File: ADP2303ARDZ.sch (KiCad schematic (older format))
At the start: 17 parts, among them P1 CONN_01X03, P2 CONN_01X03, U1 ADP2303ARDZ-5.0, U2 MCP1825S

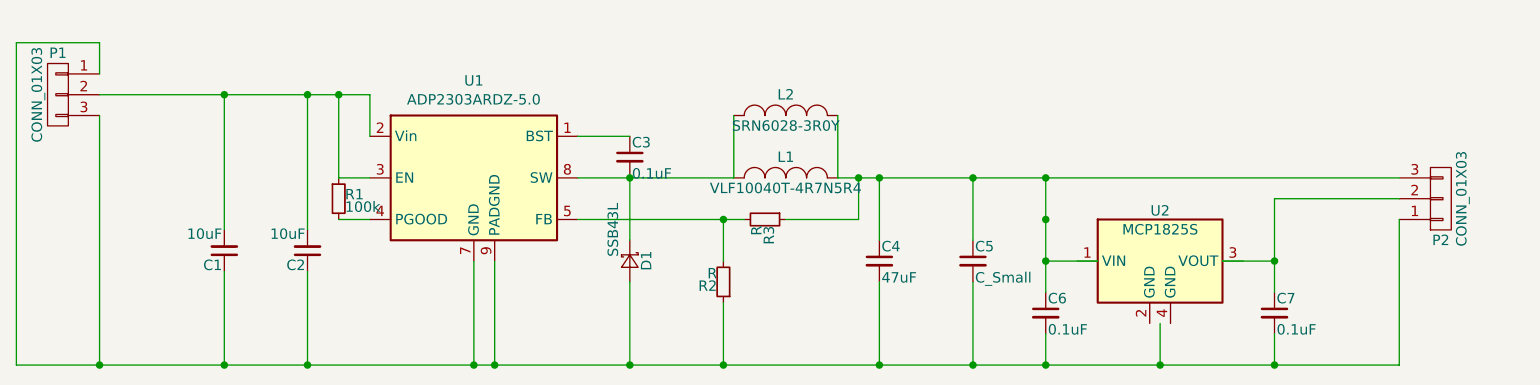
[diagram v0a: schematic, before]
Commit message: Changed design to use local componenet libs
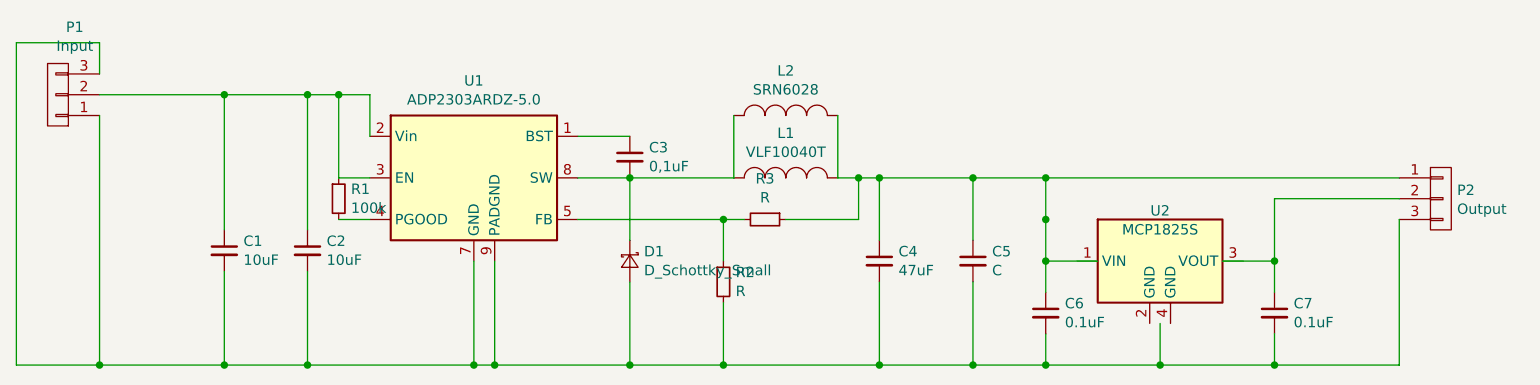
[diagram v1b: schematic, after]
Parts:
- C1, C2, C4, C6, C7: footprint Capacitor_SMD:C_0603_1608Metric_Pad0.84x1.00mm_HandSolder -> (none)
- C3: value 0.1uF -> 0,1uF; footprint Capacitor_SMD:C_0603_1608Metric_Pad0.84x1.00mm_HandSolder -> (none)
- C5: value C_Small -> C; footprint Capacitor_SMD:C_0603_1608Metric_Pad0.84x1.00mm_HandSolder -> (none)
- D1: value SSB43L -> D_Schottky_Small; footprint Diode_SMD:D_SMB_Handsoldering -> (none)
- L1: value VLF10040T-4R7N5R4 -> VLF10040T; footprint Inductor_SMD:L_TDK_VLF10040 -> (none)
- L2: value SRN6028-3R0Y -> SRN6028; footprint Inductor_SMD:L_Bourns-SRN6028 -> (none)
- P1: value CONN_01X03 -> Input; footprint Conn_PinSocket_2.54mm:PinSocket_1x03_P2.54mm_Vertical -> (none)
- P2: value CONN_01X03 -> Output; footprint Conn_PinSocket_2.54mm:PinSocket_1x03_P2.54mm_Vertical -> (none)
- R1, R2, R3: footprint Resistor_SMD:R_0603_1608Metric_Pad0.84x1.00mm_HandSolder -> (none)
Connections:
- wire segments 41 -> 65

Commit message: Selected local footprints for the design
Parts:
- C1, C2, C3, C4, C5, C6, C7: footprint (none) -> footprints:C_0603_1608Metric
- D1: footprint (none) -> footprints:D_SMB_Handsoldering
- L1: footprint (none) -> footprints:L_TDK_VLF10040
- L2: footprint (none) -> footprints:L_Bourns-SRN6028
- P1, P2: footprint (none) -> footprints:PinSocket_1x03_P2.54mm_Vertical
- R1, R2, R3: footprint (none) -> footprints:R_0603_1608Metric
- U1: footprint Housings_SOIC:SOIC-8-1EP_3.9x4.9mm_Pitch1.27mm -> footprints:SOIC-8-1EP_3.9x4.9mm_Pitch1.27mm
- U2: footprint (none) -> footprints:SOT-223
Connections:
- wire segments 65 -> 41
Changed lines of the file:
@@
 Connection ~ 5250 4300
 Wire Wire Line
-	6550 3400 6800 3400
-Wire Wire Line
-	6800 3400 7300 3400
+	6550 3400 7300 3400
 Wire Wire Line
 	6800 3200 6550 3200
@@
 	7300 3400 7300 3100
 Wire Wire Line
-	7800 3400 7900 3400
-Wire Wire Line
-	7900 3400 8000 3400
-Wire Wire Line
-	8000 3400 8450 3400
-Wire Wire Line
-	8450 3400 8800 3400
-Wire Wire Line
-	8800 3400 10500 3400
+	7800 3400 10500 3400
 Wire Wire Line
 	7800 3400 7800 3100
@@
 	8800 3800 9050 3800
 Wire Wire Line
-	8800 3400 8800 3600
-Wire Wire Line
-	8800 3600 8800 3800
-Wire Wire Line
-	8800 3800 8800 3950
+	8800 3400 8800 3950
 Connection ~ 8800 3400
 Wire Wire Line
@@
 	9650 3800 9900 3800
 Wire Wire Line
-	9900 3500 9900 3800
-Wire Wire Line
-	9900 3800 9900 3950
+	9900 3500 9900 3950
 Wire Wire Line
 	9900 3500 10500 3500
@@
 	3850 2750 3850 4300
 Wire Wire Line
-	3850 4300 4250 4300
-Wire Wire Line
-	4250 4300 4850 4300
-Wire Wire Line
-	4850 4300 5250 4300
-Wire Wire Line
-	5250 4300 6050 4300
-Wire Wire Line
-	6050 4300 6150 4300
-Wire Wire Line
-	6150 4300 6800 4300
-Wire Wire Line
-	6800 4300 7250 4300
-Wire Wire Line
-	7250 4300 8000 4300
-Wire Wire Line
-	8000 4300 8450 4300
-Wire Wire Line
-	8450 4300 8800 4300
-Wire Wire Line
-	8800 4300 9350 4300
-Wire Wire Line
-	9350 4300 9900 4300
-Wire Wire Line
-	9900 4300 10500 4300
-Wire Wire Line
-	4250 3000 4850 3000
-Wire Wire Line
-	4850 3000 5250 3000
-Wire Wire Line
-	5250 3000 5400 3000
-Wire Wire Line
-	5400 3000 5550 3000
+	3850 4300 10500 4300
+Wire Wire Line
+	4250 3000 5550 3000
 Wire Wire Line
 	5550 3000 5550 3200
@@
 Connection ~ 9350 4300
 Wire Wire Line
-	6550 3600 7250 3600
-Wire Wire Line
-	7250 3600 7350 3600
+	6550 3600 7350 3600
 Wire Wire Line
 	7550 3600 7900 3600
@@
 F 0 "P1" H 3969 2675 50  0000 C CNN
 F 1 "Input" H 3969 2766 50  0000 C CNN
-F 2 "" H 4050 3000 50  0000 C CNN
+F 2 "footprints:PinSocket_1x03_P2.54mm_Vertical" H 4050 3000 50  0001 C CNN
 F 3 "" H 4050 3000 50  0000 C CNN
 	1    4050 3000
@@
 F 0 "C1" H 4942 3796 50  0000 L CNN
 F 1 "10uF" H 4942 3705 50  0000 L CNN
-F 2 "" H 4850 3750 50  0001 C CNN
+F 2 "footprints:C_0603_1608Metric" H 4850 3750 50  0001 C CNN
 F 3 "" H 4850 3750 50  0001 C CNN
 	1    4850 3750
@@
 F 0 "C2" H 5342 3796 50  0000 L CNN
 F 1 "10uF" H 5342 3705 50  0000 L CNN
-F 2 "" H 5250 3750 50  0001 C CNN
+F 2 "footprints:C_0603_1608Metric" H 5250 3750 50  0001 C CNN
 F 3 "" H 5250 3750 50  0001 C CNN
 	1    5250 3750
@@
 F 0 "R1" H 5459 3546 50  0000 L CNN
 F 1 "100k" H 5459 3455 50  0000 L CNN
-F 2 "" H 5400 3500 50  0001 C CNN
+F 2 "footprints:R_0603_1608Metric" H 5400 3500 50  0001 C CNN
 F 3 "" H 5400 3500 50  0001 C CNN
 	1    5400 3500
@@
 F 0 "U1" H 6050 3867 50  0000 C CNN
 F 1 "ADP2303ARDZ-5.0" H 6050 3776 50  0000 C CNN
-F 2 "Housings_SOIC:SOIC-8-1EP_3.9x4.9mm_Pitch1.27mm" H 6200 3050 50  0001 L CNN
+F 2 "footprints:SOIC-8-1EP_3.9x4.9mm_Pitch1.27mm" H 6200 3050 50  0001 L CNN
 F 3 "http://www.analog.com/media/en/technical-documentation/data-sheets/ADP2302_2303.pdf" H 5850 4000 50  0001 C CNN
 	1    6050 3400
@@
 F 0 "C3" H 6892 3346 50  0000 L CNN
 F 1 "0,1uF" H 6892 3255 50  0000 L CNN
-F 2 "" H 6800 3300 50  0001 C CNN
+F 2 "footprints:C_0603_1608Metric" H 6800 3300 50  0001 C CNN
 F 3 "" H 6800 3300 50  0001 C CNN
 	1    6800 3300
@@
 F 0 "D1" V 6754 3868 50  0000 L CNN
 F 1 "D_Schottky_Small" V 6845 3868 50  0000 L CNN
-F 2 "" V 6800 3800 50  0001 C CNN
+F 2 "footprints:D_SMB_Handsoldering" V 6800 3800 50  0001 C CNN
 F 3 "" V 6800 3800 50  0001 C CNN
 	1    6800 3800
@@
 F 0 "R2" H 7309 3946 50  0000 L CNN
 F 1 "R" H 7309 3855 50  0000 L CNN
-F 2 "" H 7250 3900 50  0001 C CNN
+F 2 "footprints:R_0603_1608Metric" H 7250 3900 50  0001 C CNN
 F 3 "" H 7250 3900 50  0001 C CNN
 	1    7250 3900
@@
 F 0 "R3" V 7254 3600 50  0000 C CNN
 F 1 "R" V 7345 3600 50  0000 C CNN
-F 2 "" H 7450 3600 50  0001 C CNN
+F 2 "footprints:R_0603_1608Metric" H 7450 3600 50  0001 C CNN
 F 3 "" H 7450 3600 50  0001 C CNN
 	1    7450 3600
@@
 F 0 "L1" H 7550 3615 50  0000 C CNN
 F 1 "VLF10040T" H 7550 3524 50  0000 C CNN
-F 2 "" H 7550 3400 50  0000 C CNN
+F 2 "footprints:L_TDK_VLF10040" H 7550 3400 50  0001 C CNN
 F 3 "" H 7550 3400 50  0000 C CNN
 	1    7550 3400
@@
 F 0 "L2" H 7550 3315 50  0000 C CNN
 F 1 "SRN6028" H 7550 3224 50  0000 C CNN
-F 2 "" H 7550 3100 50  0000 C CNN
+F 2 "footprints:L_Bourns-SRN6028" H 7550 3100 50  0001 C CNN
 F 3 "" H 7550 3100 50  0000 C CNN
 	1    7550 3100
@@
 F 0 "C4" H 8092 3846 50  0000 L CNN
 F 1 "47uF" H 8092 3755 50  0000 L CNN
-F 2 "" H 8000 3800 50  0001 C CNN
+F 2 "footprints:C_0603_1608Metric" H 8000 3800 50  0001 C CNN
 F 3 "" H 8000 3800 50  0001 C CNN
 	1    8000 3800
@@
 F 0 "C5" H 8542 3846 50  0000 L CNN
 F 1 "C" H 8542 3755 50  0000 L CNN
-F 2 "" H 8450 3800 50  0001 C CNN
+F 2 "footprints:C_0603_1608Metric" H 8450 3800 50  0001 C CNN
 F 3 "" H 8450 3800 50  0001 C CNN
 	1    8450 3800
@@
 F 0 "C6" H 8892 4096 50  0000 L CNN
 F 1 "0.1uF" H 8892 4005 50  0000 L CNN
-F 2 "" H 8800 4050 50  0001 C CNN
+F 2 "footprints:C_0603_1608Metric" H 8800 4050 50  0001 C CNN
 F 3 "" H 8800 4050 50  0001 C CNN
 	1    8800 4050
@@
 F 0 "C7" H 9992 4096 50  0000 L CNN
 F 1 "0.1uF" H 9992 4005 50  0000 L CNN
-F 2 "" H 9900 4050 50  0001 C CNN
+F 2 "footprints:C_0603_1608Metric" H 9900 4050 50  0001 C CNN
 F 3 "" H 9900 4050 50  0001 C CNN
 	1    9900 4050
@@
 F 0 "U2" H 9350 4042 50  0000 C CNN
 F 1 "MCP1825S" H 9350 3951 50  0000 C CNN
-F 2 "" H 9250 3950 50  0001 C CNN
+F 2 "footprints:SOT-223" H 9250 3950 50  0001 C CNN
 F 3 "http://ww1.microchip.com/downloads/en/devicedoc/22056b.pdf" H 9350 4050 50  0001 C CNN
 	1    9350 3800
@@
 F 0 "P2" H 10778 3541 50  0000 L CNN
 F 1 "Output" H 10778 3450 50  0000 L CNN
-F 2 "" H 10700 3500 50  0000 C CNN
+F 2 "footprints:PinSocket_1x03_P2.54mm_Vertical" H 10700 3500 50  0001 C CNN
 F 3 "" H 10700 3500 50  0000 C CNN
 	1    10700 3500

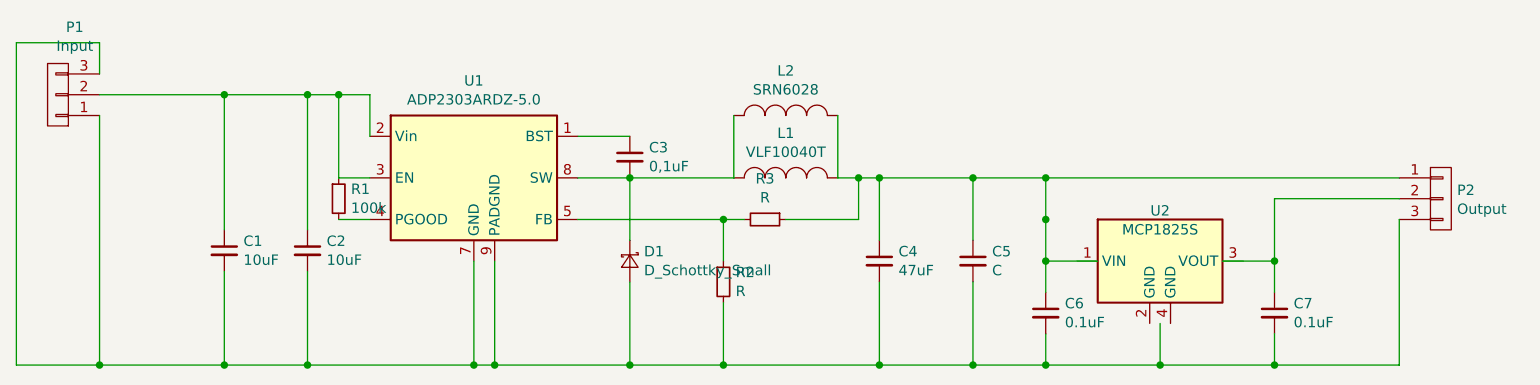
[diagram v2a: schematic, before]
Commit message: Added value for diode
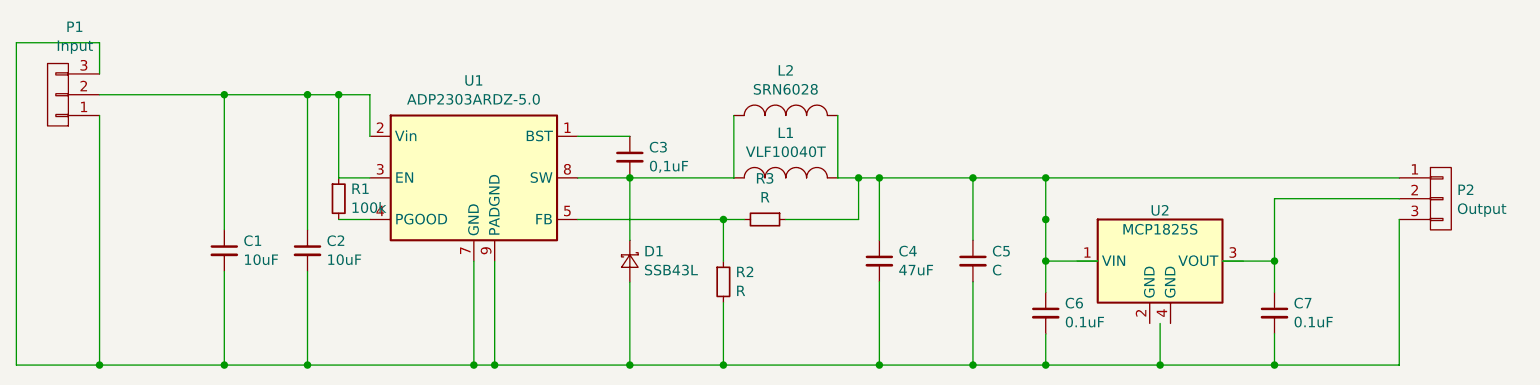
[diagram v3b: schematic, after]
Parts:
- D1: value D_Schottky_Small -> SSB43L
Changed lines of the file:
@@
 P 6800 3800
 F 0 "D1" V 6754 3868 50  0000 L CNN
-F 1 "D_Schottky_Small" V 6845 3868 50  0000 L CNN
+F 1 "SSB43L" V 6845 3868 50  0000 L CNN
 F 2 "footprints:D_SMB_Handsoldering" V 6800 3800 50  0001 C CNN
 F 3 "" V 6800 3800 50  0001 C CNN

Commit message: Fully connected but no Gnd plane as yet
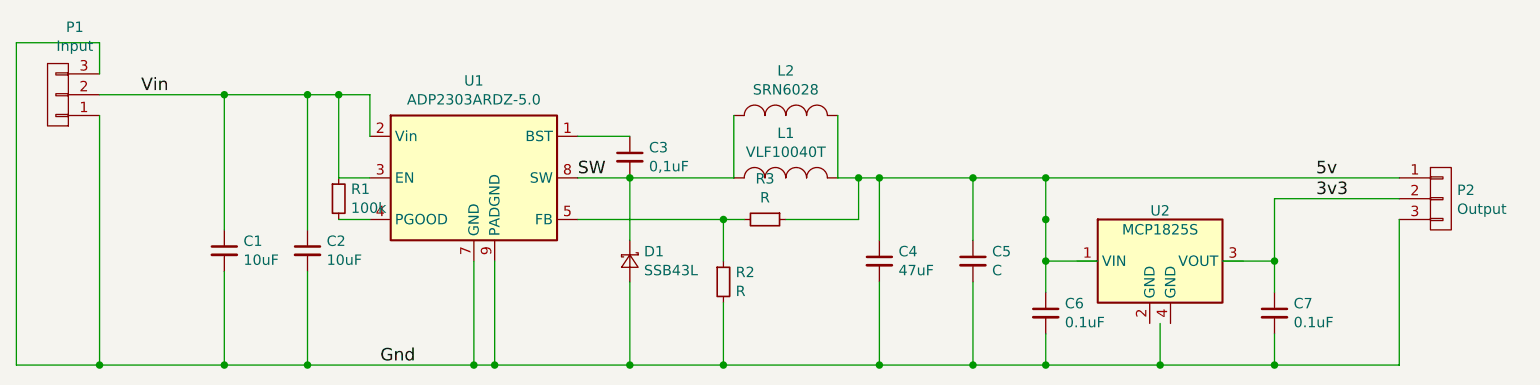
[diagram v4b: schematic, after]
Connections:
- net labels added: 3v3, 5v, Gnd, SW, Vin
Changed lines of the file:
@@
 	1    0    0    -1
 $EndComp
+Text Label 6550 3400 0    60   ~ 0
+SW
+Text Label 4450 3000 0    60   ~ 0
+Vin
+Text Label 10100 3400 0    60   ~ 0
+5v
+Text Label 10100 3500 0    60   ~ 0
+3v3
+Text Label 5600 4300 0    60   ~ 0
+Gnd
 $EndSCHEMATC

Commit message: Added 0805 Cap Footprint
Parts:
- C1, C2, C3, C4, C5, C6, C7: symbol C_Small -> c_small:C_Small
- D1: symbol D_Schottky_Small -> d_schottky_small:D_Schottky_Small
- L1, L2: symbol INDUCTOR_SMALL -> inductor_small:INDUCTOR_SMALL
- P1, P2: symbol CONN_01X03 -> conn_01x03:CONN_01X03
- R1, R2, R3: symbol R_Small -> r_small:R_Small
- U1: symbol ADP2303ARDZ-5.0 -> adp2302ardz:ADP2303ARDZ-5.0
- U2: symbol MCP1825S -> mcp1825s:MCP1825S
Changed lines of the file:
@@
-EESchema Schematic File Version 3
-LIBS:adp2302ardz
-LIBS:conn_01x03
-LIBS:c_small
-LIBS:d_schottky_small
-LIBS:inductor_small
-LIBS:mcp1825s
-LIBS:r_small
+EESchema Schematic File Version 4
 LIBS:ADP2303ARDZ-cache
 EELAYER 26 0
@@
 Connection ~ 7250 4300
 $Comp
-L CONN_01X03 P1
+L conn_01x03:CONN_01X03 P1
 U 1 1 5A09A5D8
 P 4050 3000
@@
 $EndComp
 $Comp
-L C_Small C1
+L c_small:C_Small C1
 U 1 1 5A09A767
 P 4850 3750
@@
 $EndComp
 $Comp
-L C_Small C2
+L c_small:C_Small C2
 U 1 1 5A09A846
 P 5250 3750
@@
 $EndComp
 $Comp
-L R_Small R1
+L r_small:R_Small R1
 U 1 1 5A09AB04
 P 5400 3500
@@
 $EndComp
 $Comp
-L ADP2303ARDZ-5.0 U1
+L adp2302ardz:ADP2303ARDZ-5.0 U1
 U 1 1 5A09AC83
 P 6050 3400
@@
 $EndComp
 $Comp
-L C_Small C3
+L c_small:C_Small C3
 U 1 1 5A09ADC8
 P 6800 3300
@@
 $EndComp
 $Comp
-L D_Schottky_Small D1
+L d_schottky_small:D_Schottky_Small D1
 U 1 1 5A09AF2F
 P 6800 3800
@@
 $EndComp
 $Comp
-L R_Small R2
+L r_small:R_Small R2
 U 1 1 5A09B1A3
 P 7250 3900
@@
 $EndComp
 $Comp
-L R_Small R3
+L r_small:R_Small R3
 U 1 1 5A09B1FB
 P 7450 3600
@@
 $EndComp
 $Comp
-L INDUCTOR_SMALL L1
+L inductor_small:INDUCTOR_SMALL L1
 U 1 1 5A09B461
 P 7550 3400
@@
 $EndComp
 $Comp
-L INDUCTOR_SMALL L2
+L inductor_small:INDUCTOR_SMALL L2
 U 1 1 5A09B4C5
 P 7550 3100
@@
 $EndComp
 $Comp
-L C_Small C4
+L c_small:C_Small C4
 U 1 1 5A09B81E
 P 8000 3800
@@
 $EndComp
 $Comp
-L C_Small C5
+L c_small:C_Small C5
 U 1 1 5A09B916
 P 8450 3800
@@
 $EndComp
 $Comp
-L C_Small C6
+L c_small:C_Small C6
 U 1 1 5A09BAED
 P 8800 4050
@@
 $EndComp
 $Comp
-L C_Small C7
+L c_small:C_Small C7
 U 1 1 5A09BBBF
 P 9900 4050
@@
 $EndComp
 $Comp
-L MCP1825S U2
+L mcp1825s:MCP1825S U2
 U 1 1 5A09BDA1
 P 9350 3800
@@
 $EndComp
 $Comp
-L CONN_01X03 P2
+L conn_01x03:CONN_01X03 P2
 U 1 1 5A09C2B2
 P 10700 3500

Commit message: Change layout to use 0805 Cap
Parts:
- C4, C5: footprint footprints:C_0603_1608Metric -> footprints:C_0805_2012Metric
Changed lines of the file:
@@
 F 0 "C4" H 8092 3846 50  0000 L CNN
 F 1 "47uF" H 8092 3755 50  0000 L CNN
-F 2 "footprints:C_0603_1608Metric" H 8000 3800 50  0001 C CNN
+F 2 "footprints:C_0805_2012Metric" H 8000 3800 50  0001 C CNN
 F 3 "" H 8000 3800 50  0001 C CNN
 	1    8000 3800
@@
 F 0 "C5" H 8542 3846 50  0000 L CNN
 F 1 "C" H 8542 3755 50  0000 L CNN
-F 2 "footprints:C_0603_1608Metric" H 8450 3800 50  0001 C CNN
+F 2 "footprints:C_0805_2012Metric" H 8450 3800 50  0001 C CNN
 F 3 "" H 8450 3800 50  0001 C CNN
 	1    8450 3800
